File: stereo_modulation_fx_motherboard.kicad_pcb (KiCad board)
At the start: 2 copper layers, 101.6 x 139.7 mm, 48 parts, among them J1 dry_out_A, J2 CV_out_A, J3 wet_in_A, J4 rez_CV_out_A, J5 dry_out_B, J6 CV_out_B, J7 wet_in_B, J8 rez_CV_out_B, SW1 sweep_mode, SW2 invert_B, U1 Teensy3.2, U2 CD74HC4067M, U3 MCP4812, U4 MCP4812, U5 TL072, U6 TL072, U7 CC3-0512DF-E

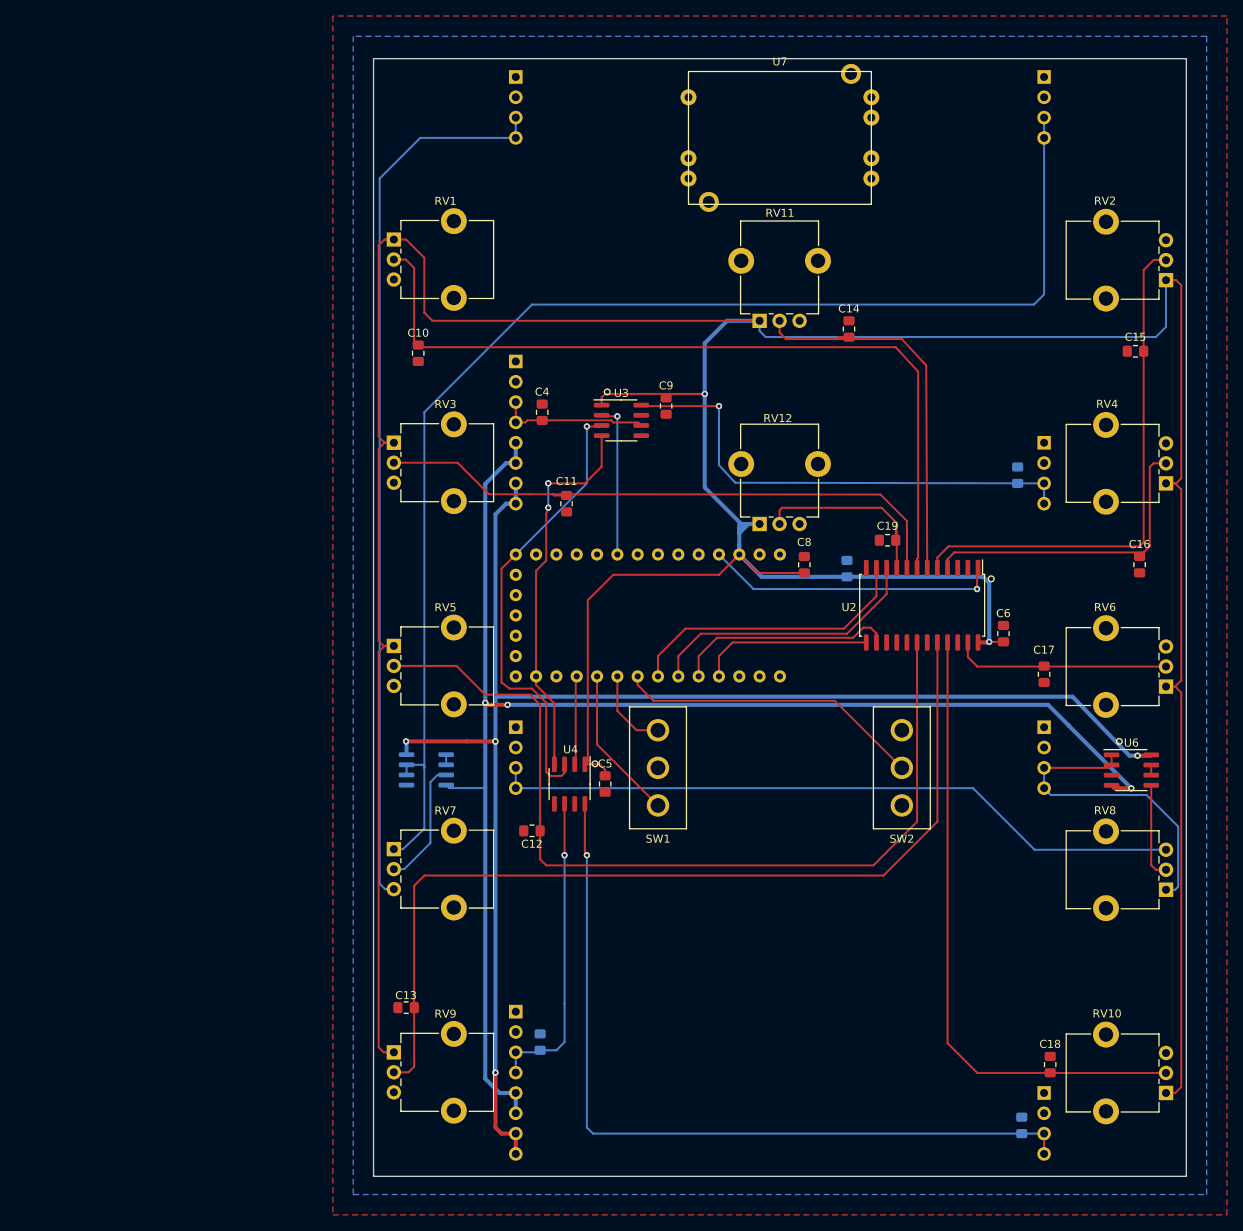
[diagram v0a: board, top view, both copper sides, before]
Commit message: add wet/dry mix inverter, tidy up board, NOT DONE DO NOT ORDER BOARDS!
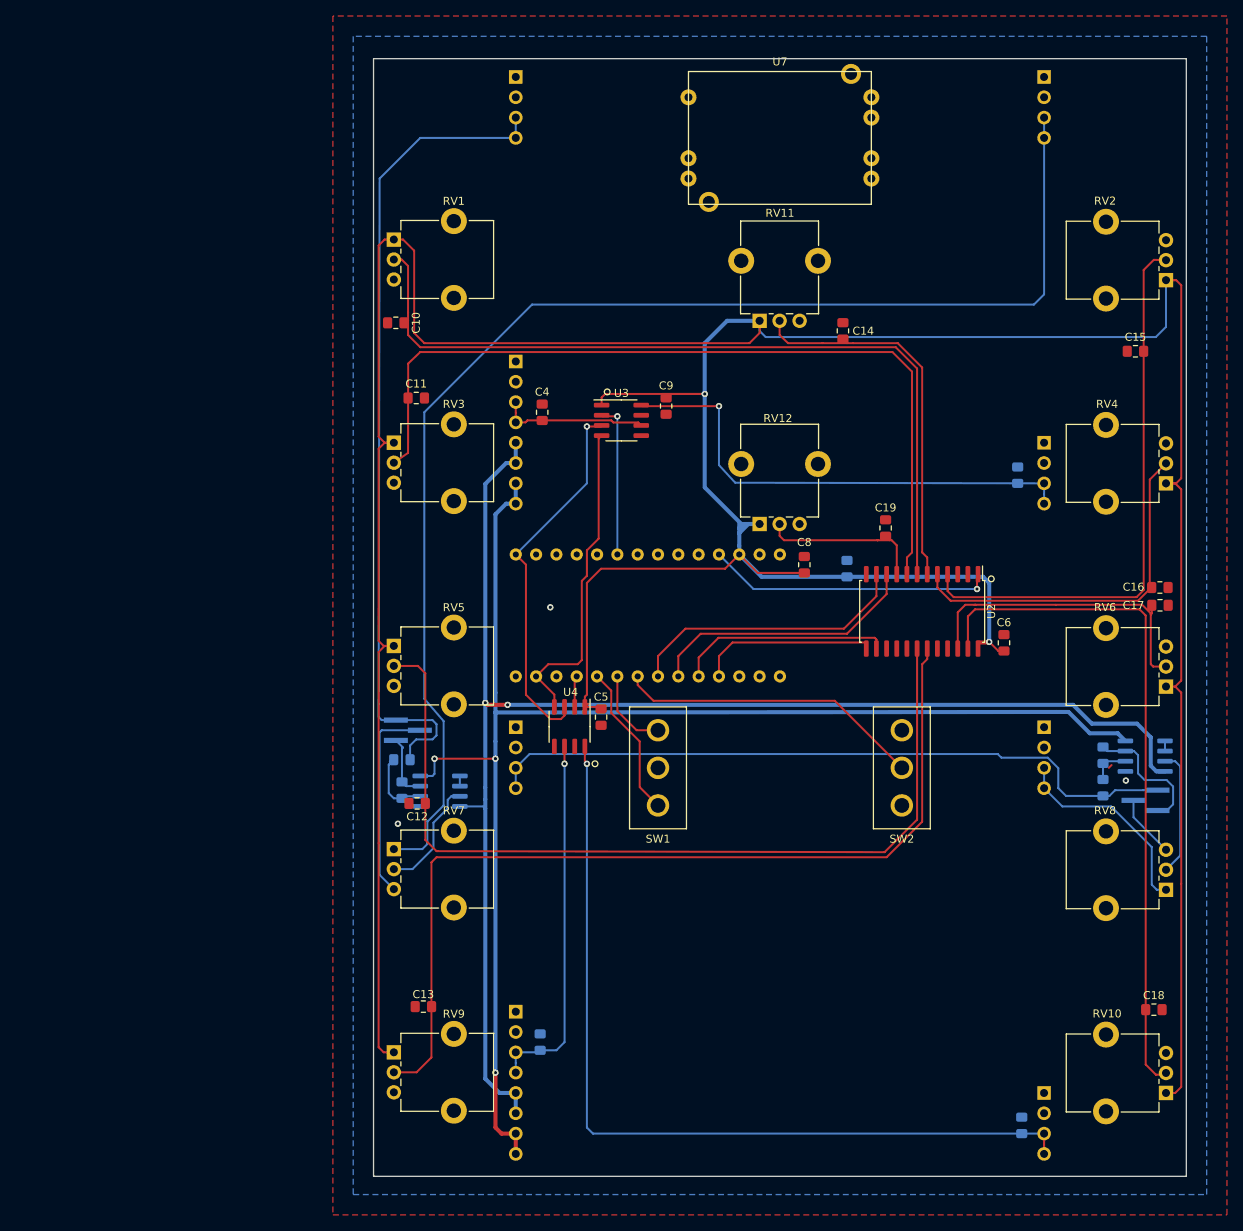
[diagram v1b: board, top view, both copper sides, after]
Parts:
- added JP1: mix polarity A, Connector_PinHeader_1.27mm:PinHeader_1x03_P1.27mm_Vertical_SMD_Pin1Left, B.Cu at (29.7, 109.6)
- added JP2: mix polarity B, Connector_PinHeader_1.27mm:PinHeader_1x03_P1.27mm_Vertical_SMD_Pin1Left, B.Cu at (121.9, 118.4)
- added R1: 10k, Resistor_SMD:R_0805_2012Metric_Pad1.15x1.40mm_HandSolder, B.Cu at (116.6, 116.8)
- added R2: 10k, Resistor_SMD:R_0805_2012Metric_Pad1.15x1.40mm_HandSolder, B.Cu at (28.9, 113.3)
- added R3: 10k, Resistor_SMD:R_0805_2012Metric_Pad1.15x1.40mm_HandSolder, B.Cu at (116.6, 112.7)
- added R4: 10k, Resistor_SMD:R_0805_2012Metric_Pad1.15x1.40mm_HandSolder, B.Cu at (29.0, 117.1)
- U6: moved to B.Cu
- moved C11 23.0 mm to (30.7, 68.1), turned to 0 degrees
- moved C17 16.9 mm to (123.7, 94.0), turned to 0 degrees
- moved C12 14.8 mm to (30.9, 118.7)
- moved C18 14.7 mm to (122.9, 144.5), turned to 0 degrees
- moved C5 8.38 mm to (53.8, 108.0)
- moved U4 7.18 mm to (49.9, 109.2)
- moved C10 4.72 mm to (28.2, 58.7), turned to 180 degrees
- moved C16 3.82 mm to (123.7, 91.8), turned to 0 degrees
- moved U5 3.17 mm to (33.7, 117.2)
- moved U6 2.45 mm to (121.9, 112.8), turned to 180 degrees
- moved C13 2.16 mm to (31.6, 144.1)
- moved C19 1.55 mm to (89.4, 84.3), turned to 90 degrees
- moved C6 1.14 mm to (104.2, 98.7)
- moved C14 0.80 mm to (84.1, 59.7)
- moved U2 0.76 mm to (94.0, 94.7)
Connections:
- RV7 pad 3: wet_in_A -> Net-(JP1-Pad2)
- RV8 pad 3: wet_in_B -> Net-(JP2-Pad2)
- U2 pad 19: Net-(U2-Pad19) -> rez_A
- U2 pad 20: rez_A -> Net-(U2-Pad20)
- U2 pad 21: rez_B -> Net-(U2-Pad21)
- U2 pad 22: Net-(U2-Pad22) -> shape_B
- U2 pad 23: shape_B -> rez_B
- U2 pad 4: depth_B -> rate_B
- U2 pad 5: rate_B -> depth_B
- U5 pad 5: Net-(U5-Pad5) -> GNDREF
- U5 pad 6: dry_out_A -> Net-(R2-Pad1)
- U5 pad 7: dry_out_A -> Net-(JP1-Pad1)
- U6 pad 1: dry_out_B -> Net-(U6-Pad1)
- U6 pad 2: dry_out_B -> Net-(U6-Pad1)
- U6 pad 3: Net-(U6-Pad3) -> Net-(RV8-Pad2)
- U6 pad 5: Net-(RV8-Pad2) -> GNDREF
- U6 pad 6: Net-(U6-Pad6) -> Net-(R1-Pad1)
- U6 pad 7: Net-(U6-Pad6) -> Net-(JP2-Pad3)
- U7 pad 5: Net-(U7-Pad5) -> GNDREF
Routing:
- net depth_A: track 74.8 -> 102.7 mm
- net Net-(JP1-Pad2): track 0.00 -> 25.5 mm
- net Net-(JP2-Pad3): track 0.00 -> 16.6 mm
- net dry_out_B: track 40.4 -> 25.8 mm
- net shape_B: track 27.1 -> 38.4 mm
- net SPI_CLK: track 57.3 -> 47.0 mm
- net Net-(R2-Pad1): track 0.00 -> 9.66 mm
- net wet_in_A: track 111.9 -> 103.6 mm
- net Net-(JP1-Pad1): track 0.00 -> 8.11 mm
- net Net-(JP2-Pad2): track 0.00 -> 7.86 mm
- net SPI_DATA_OUT: track 48.0 -> 40.4 mm, vias 2 -> 0
- net depth_B: track 39.2 -> 46.8 mm
- net CV_out_B: track 100.6 -> 107.7 mm
- net rez_CV_out_B: track 39.0 -> 46.1 mm
- net DAC_B_select: track 11.2 -> 4.27 mm
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
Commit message: add input buffers, misc tidy up, NOT DONE DO NOT ORDER BOARDS!
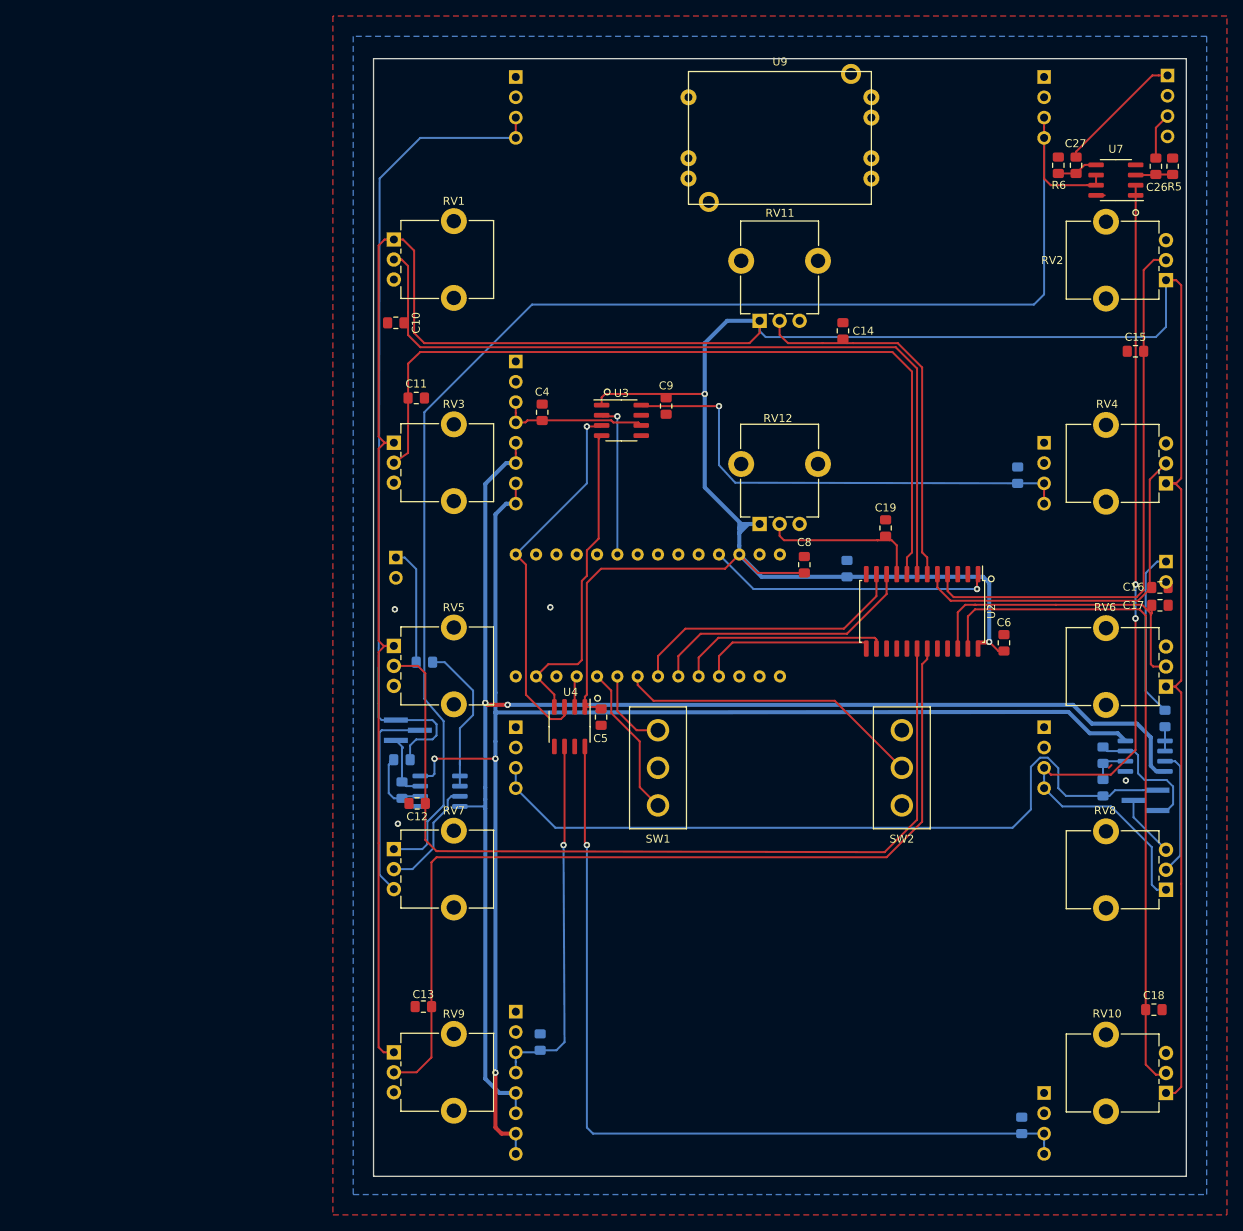
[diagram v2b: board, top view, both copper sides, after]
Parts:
- added C26: 47nF, Capacitor_SMD:C_0805_2012Metric_Pad1.15x1.40mm_HandSolder, F.Cu at (123.2, 39.1)
- added C27: 47nF, Capacitor_SMD:C_0805_2012Metric_Pad1.15x1.40mm_HandSolder, F.Cu at (113.2, 39.0)
- added J10: Conn_01x04_Male, Connector_PinHeader_2.54mm:PinHeader_1x04_P2.54mm_Vertical, B.Cu at (124.7, 27.7)
- added J11: Conn_01x02_Male, Connector_PinHeader_2.54mm:PinHeader_1x02_P2.54mm_Vertical, B.Cu at (124.5, 88.5)
- added J12: Conn_01x02_Male, Connector_PinHeader_2.54mm:PinHeader_1x02_P2.54mm_Vertical, B.Cu at (28.2, 88.0)
- added R5: 1M, Resistor_SMD:R_0805_2012Metric_Pad1.15x1.40mm_HandSolder, F.Cu at (125.3, 39.1)
- added R6: 1M, Resistor_SMD:R_0805_2012Metric_Pad1.15x1.40mm_HandSolder, F.Cu at (111.0, 39.0)
- added R7: 220, Resistor_SMD:R_0805_2012Metric_Pad1.15x1.40mm_HandSolder, B.Cu at (31.8, 101.1)
- added R8: 220, Resistor_SMD:R_0805_2012Metric_Pad1.15x1.40mm_HandSolder, B.Cu at (124.3, 108.1)
- added U7: TL072, Package_SO:SOIC-8_3.9x4.9mm_P1.27mm, F.Cu at (118.2, 40.8)
- renumbered U7 to U9
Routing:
- net dry_out_B: track 25.8 -> 109.5 mm, vias 0 -> 2
- net output_B: track 0.00 -> 21.3 mm
- net Net-(R7-Pad2): track 1.27 -> 19.5 mm
- net input_A: track 0.00 -> 16.1 mm
- net output_A: track 0.00 -> 14.8 mm
- net dry_out_A: track 165.8 -> 180.1 mm
- net wet_in_B: track 87.4 -> 95.3 mm
- net input_B: track 0.00 -> 5.86 mm
- net Net-(C27-Pad1): track 0.00 -> 5.17 mm
- net Net-(C26-Pad1): track 0.00 -> 4.64 mm
- net Net-(R8-Pad2): track 1.27 -> 3.05 mm
- net +9V: track 179.3 -> 180.4 mm
- net GNDREF: vias 3 -> 4
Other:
- board text added: "A in"
- board text added: "B in"
- board text added: "out A"
- board text added: "out B"

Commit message: change DACs to MCP4822, misc tidy up, DO NOT ORDER BOARDS!
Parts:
- U3, U4: value MCP4812 -> MCP4822
- moved C9 15.3 mm to (49.6, 78.1), turned to 0 degrees
- moved U3 13.5 mm to (48.9, 82.0)
- moved J11 2.29 mm to (124.5, 86.2)
- moved C4 0.24 mm to (46.5, 70.1)
- moved U4 0.06 mm to (49.9, 109.2)
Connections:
- U1 pad 22: Net-(U1-Pad22) -> DAC_A_select
- U1 pad 25: DAC_A_select -> Net-(U1-Pad25)
- U9 pad 2: Net-(U9-Pad2) -> Net-(C20-Pad2)
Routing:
- net SPI_DATA_OUT: track 40.4 -> 24.5 mm
- net SPI_CLK: track 47.0 -> 32.3 mm, vias 1 -> 0
- net +3V3: track 491.4 -> 478.6 mm, vias 2 -> 1
- net DAC_A_select: track 19.3 -> 7.74 mm, vias 1 -> 0
- net CV_out_A: track 61.3 -> 65.7 mm
- net rez_CV_out_A: track 18.6 -> 21.4 mm
- net output_B: track 21.3 -> 23.1 mm
